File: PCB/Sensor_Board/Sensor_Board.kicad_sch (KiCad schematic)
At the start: 4 parts, among them J1 Conn_01x08_Socket, J2 Conn_01x06_Socket, J3 Conn_01x04_Socket, J4 Conn_01x07_Socket

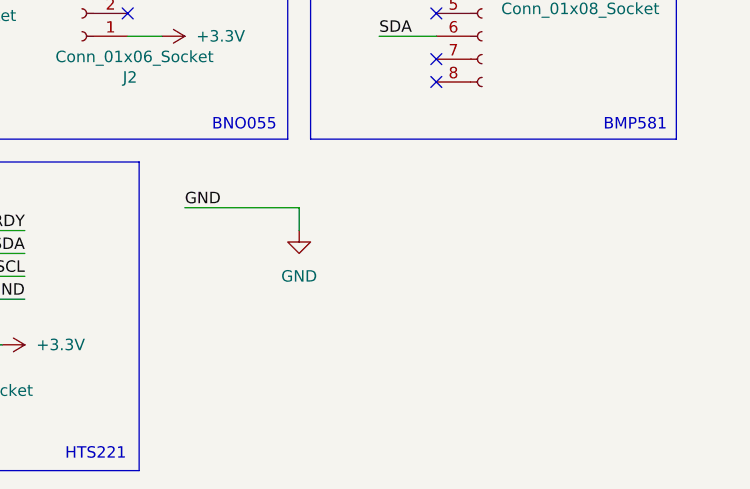
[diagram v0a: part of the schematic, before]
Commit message: Added Module
Added Ult. GPS Breakout V3
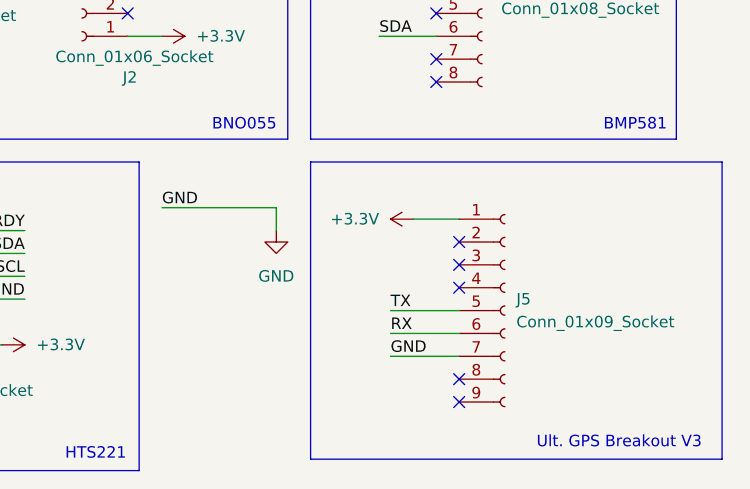
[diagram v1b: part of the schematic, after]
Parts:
- added J5: Conn_01x09_Socket, Connector_PinSocket_2.54mm:PinSocket_1x09_P2.54mm_Vertical, symbol Connector:Conn_01x09_Socket
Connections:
- net +3.3V: now also J5.1 (Pin_1)
- net GND: now also J5.7 (Pin_7)
- new net RX: J5.6 (Pin_6)
- new net TX: J5.5 (Pin_5)
- no-connect marks 12 -> 17
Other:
- note added: "Ult. GPS Breakout V3"

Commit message: added connector
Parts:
- added J6: SE2-30, SE2-30:SE2-30, symbol SE2-30:SE2-30
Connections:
- net +3.3V: now also J6. (GND)
- net GND: now also J6. (GND)
- net RX: now also J6. (GND)
- net SCL: now also J6. (GND)
- net SDA: now also J6. (GND)
- net TX: now also J6. (GND)

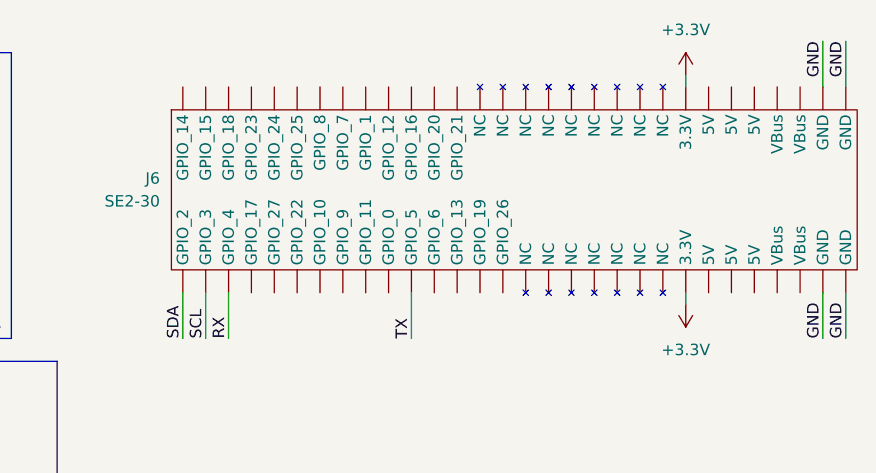
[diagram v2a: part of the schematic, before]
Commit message: routed all traces to connector
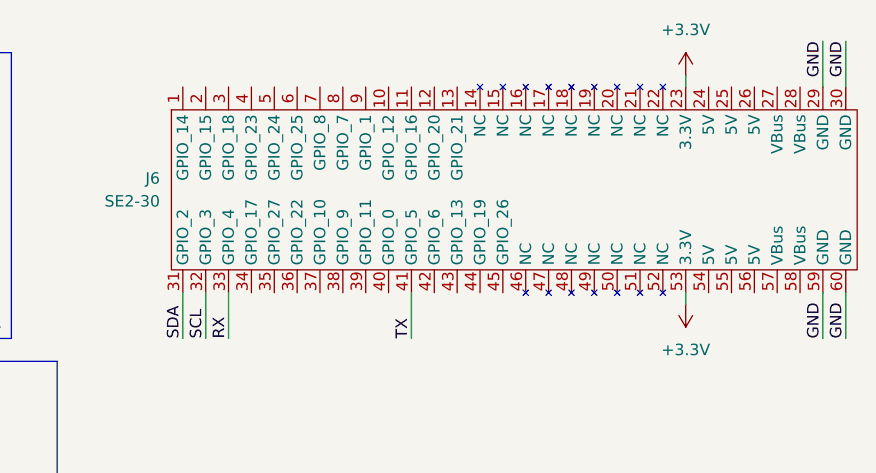
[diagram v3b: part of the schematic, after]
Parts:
- J6: footprint SE2-30:SE2-30 -> SE2-30_Footprint:SE2-30
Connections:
- net +3.3V: now also J6.23 (3.3V), J6.53 (3.3V); no longer J6. (GND)
- net GND: now also J6.29 (GND), J6.30 (GND), J6.59 (GND), J6.60 (GND); no longer J6. (GND)
- net RX: now also J6.33 (GPIO_4); no longer J6. (GND)
- net SCL: now also J6.32 (GPIO_3); no longer J6. (GND)
- net SDA: now also J6.31 (GPIO_2); no longer J6. (GND)
- net TX: now also J6.41 (GPIO_5); no longer J6. (GND)
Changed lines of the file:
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@@
 			)
 		)
-		(property "Footprint" "SE2-30:SE2-30"
+		(property "Footprint" "SE2-30_Footprint:SE2-30"
 			(at 166.37 21.59 0)
 			(effects
@@
 			)
 		)
-		(pin ""
+		(pin "36"
 		)
-		(pin ""
+		(pin "5"
 		)
-		(pin ""
+		(pin "26"
 		)
-		(pin ""
+		(pin "21"
 		)
-		(pin ""
+		(pin "58"
 		)
-		(pin ""
+		(pin "45"
 		)
-		(pin ""
+		(pin "50"
 		)
-		(pin ""
+		(pin "30"
 		)
-		(pin ""
+		(pin "53"
 		)
-		(pin ""
+		(pin "19"
 		)
-		(pin ""
+		(pin "52"
 		)
-		(pin ""
+		(pin "15"
 		)
-		(pin ""
+		(pin "44"
 		)
-		(pin ""
+		(pin "6"
 		)
-		(pin ""
+		(pin "34"
 		)
-		(pin ""
+		(pin "41"
 		)
-		(pin ""
+		(pin "51"
 		)
-		(pin ""
+		(pin "47"
 		)
-		(pin ""
+		(pin "43"
 		)
-		(pin ""
+		(pin "13"
 		)
-		(pin ""
+		(pin "46"
 		)
-		(pin ""
+		(pin "24"
 		)
-		(pin ""
+		(pin "17"
 		)
-		(pin ""
+		(pin "48"
 		)
-		(pin ""
+		(pin "18"
 		)
-		(pin ""
+		(pin "38"
 		)
-		(pin ""
+		(pin "49"
 		)
-		(pin ""
+		(pin "31"
 		)
-		(pin ""
+		(pin "39"
 		)
-		(pin ""
+		(pin "9"
 		)
-		(pin ""
+		(pin "2"
 		)
-		(pin ""
+		(pin "42"
 		)
-		(pin ""
+		(pin "10"
 		)
-		(pin ""
+		(pin "4"
 		)
-		(pin ""
+		(pin "35"
 		)
-		(pin ""
+		(pin "23"
 		)
-		(pin ""
+		(pin "7"
 		)
-		(pin ""
+		(pin "37"
 		)
-		(pin ""
+		(pin "16"
 		)
-		(pin ""
+		(pin "22"
 		)
-		(pin ""
+		(pin "14"
 		)
-		(pin ""
+		(pin "11"
 		)
-		(pin ""
+		(pin "8"
 		)
-		(pin ""
+		(pin "55"
 		)
-		(pin ""
+		(pin "3"
 		)
-		(pin ""
+		(pin "27"
 		)
-		(pin ""
+		(pin "12"
 		)
-		(pin ""
+		(pin "59"
 		)
-		(pin ""
+		(pin "20"
 		)
-		(pin ""
+		(pin "29"
 		)
-		(pin ""
+		(pin "25"
 		)
-		(pin ""
+		(pin "1"
 		)
-		(pin ""
+		(pin "57"
 		)
-		(pin ""
+		(pin "56"
 		)
-		(pin ""
+		(pin "60"
 		)
-		(pin ""
+		(pin "32"
 		)
-		(pin ""
+		(pin "40"
 		)
-		(pin ""
+		(pin "28"
 		)
-		(pin ""
+		(pin "54"
 		)
-		(pin ""
+		(pin "33"
 		)
 		(instances
